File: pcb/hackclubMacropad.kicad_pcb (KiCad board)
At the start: 2 copper layers, 77.5 x 95 mm, 25 parts, among them SW1 SW_Push, SW10 RotaryEncoder_Switch_MP, SW2 SW_Push, SW3 SW_Push, SW4 SW_Push, SW5 SW_Push, SW6 SW_Push, SW7 SW_Push, SW8 SW_Push, SW9 SW_Push, U1 MOUDLE-SEEEDUINO-XIAO

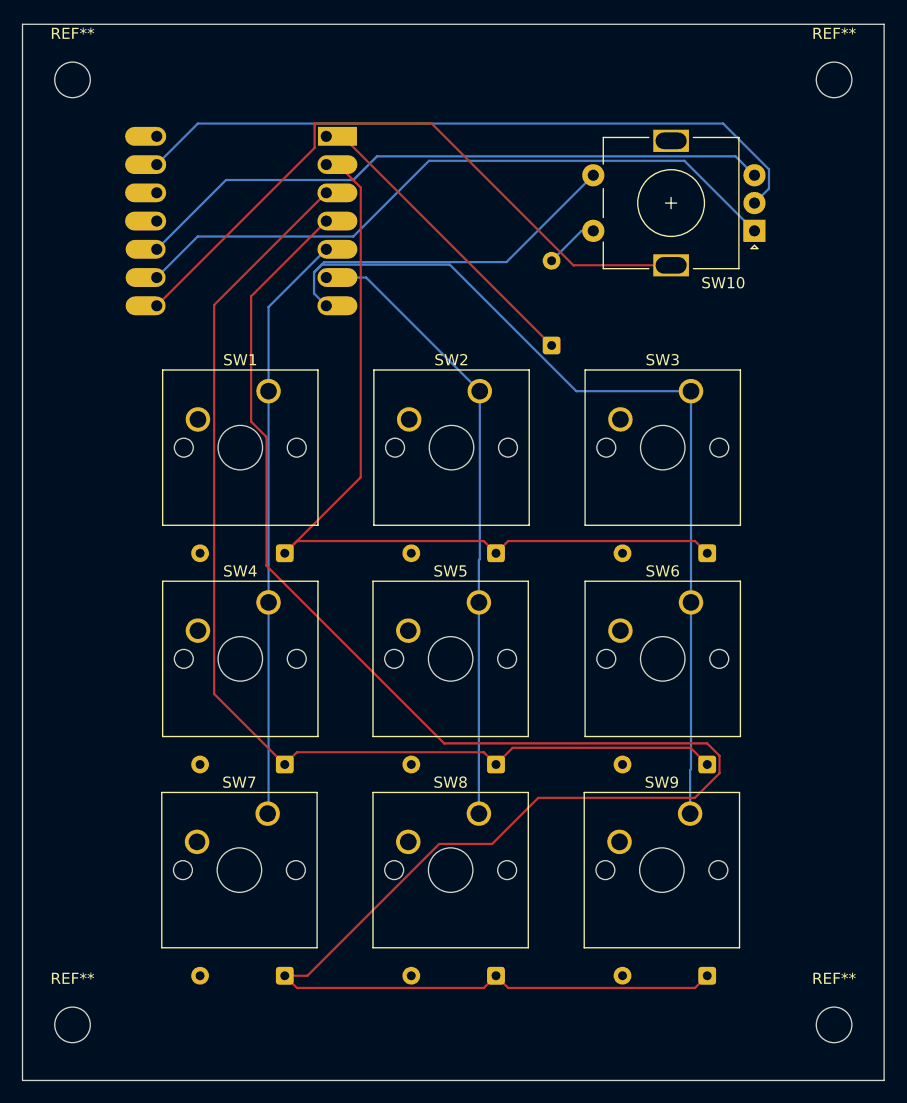
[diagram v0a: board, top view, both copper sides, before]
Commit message: updated pcb to not connect mounting pin
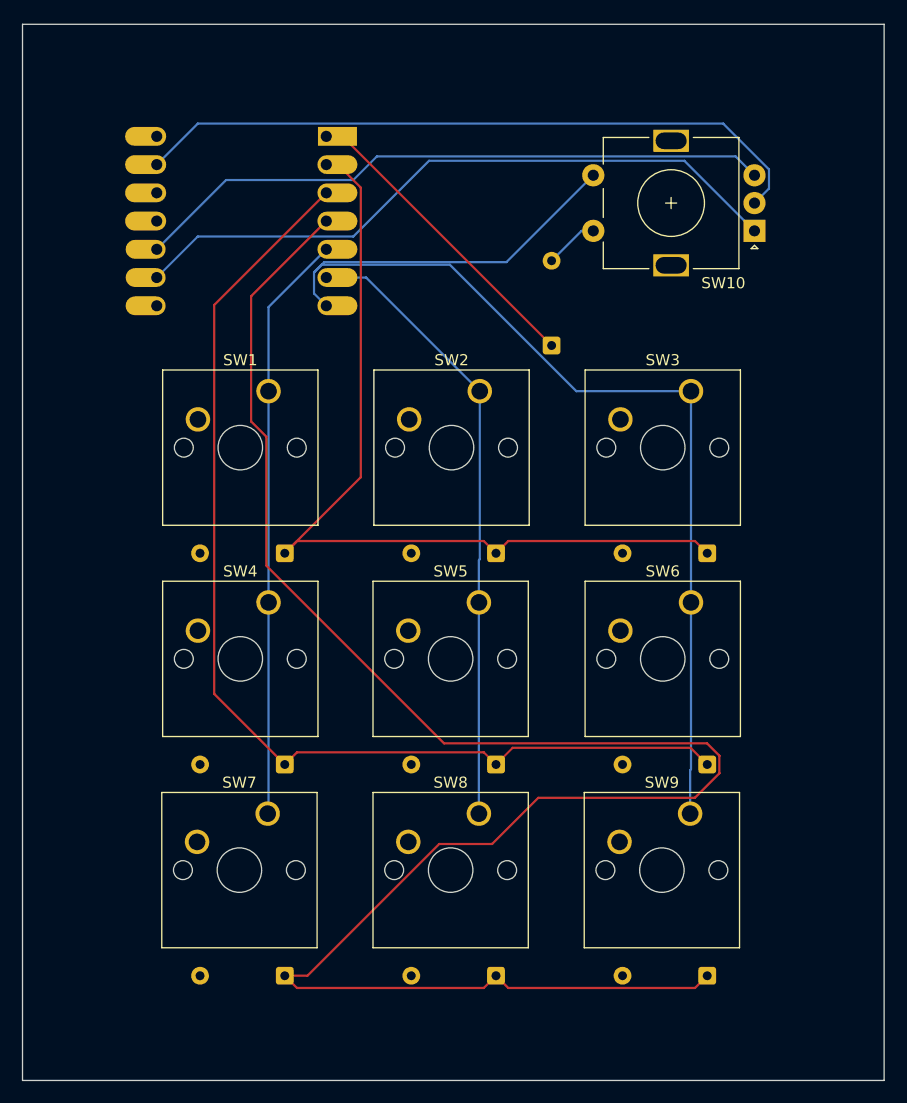
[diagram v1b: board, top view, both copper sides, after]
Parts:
- removed REF** (x4): MountingHole_3.2mm_M3, MountingHole:MountingHole_3.2mm_M3
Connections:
- SW10 pad MP: /EC11MP -> unconnected-(SW10-PadMP)
- U1 pad 8: /EC11MP -> unconnected-(U1-PB09_A7_D7_RX-Pad8)
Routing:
- net /EC11MP: track 59.6 -> 0.00 mm
